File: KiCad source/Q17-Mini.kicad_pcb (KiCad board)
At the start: 2 copper layers, 95 x 75 mm, 85 parts, among them J1 Input, Q1 FQP3N30, Q10 KSA992, Q11 BS250P, Q12 BD139, Q13 FQP3N30, Q14 IRF9610, Q15 FQA46N15, Q16 FQA36P15, Q2 KSA992, Q3 KSC1845, Q4 FQP3P20, Q5 FQP3P20, Q6 FQP3N30, Q7 KSC1845, Q8 2N7000, Q9 BS250P, U1 OPA1641

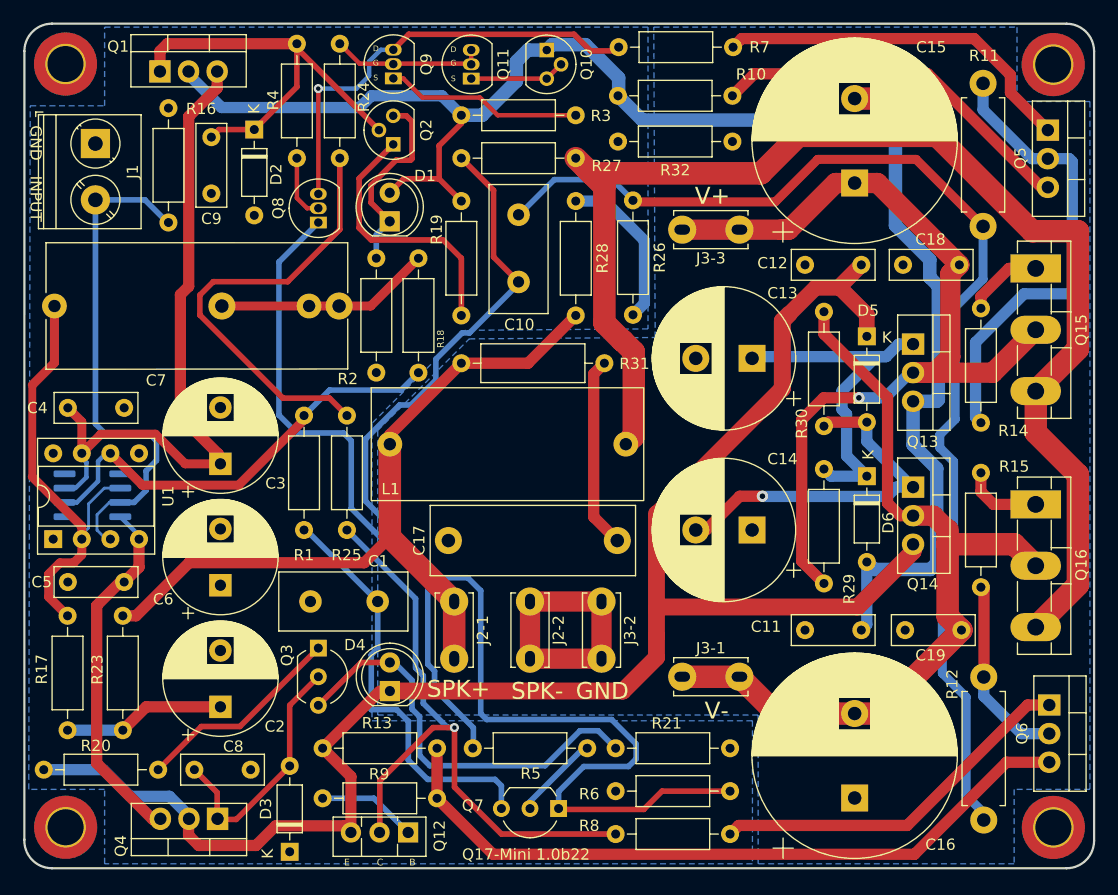
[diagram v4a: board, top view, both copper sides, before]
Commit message: Version 1.0
- Version 1.0 of Q17-Mini PCB.
- New footprint for C7 compatible with lead space of 15mm and 22.5mm.
- L1 adjusted to the correct inductance length of 22x10mm for 1.2uF (Wire: 1mm, Tube: 8mm interior, 22 turns).
- Gerber files for Q7-Mini 1.0.
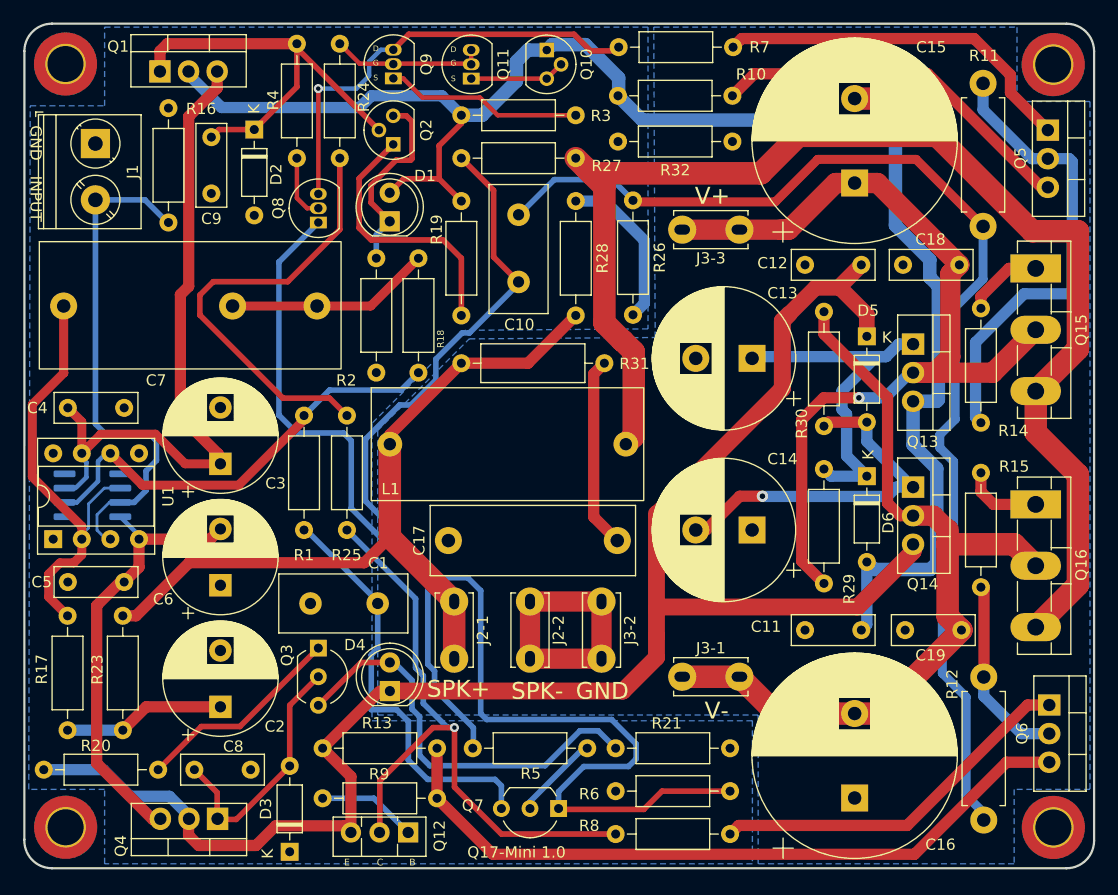
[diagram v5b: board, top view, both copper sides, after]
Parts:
- C7: footprint Capacitor_THT:C_Rect_L29.0mm_W11.0mm_P27.50mm_MKT_special -> Capacitor_THT:C_Rect_C7_Q17-Mini
- moved C7 0.94 mm to (103.3, 80.1)
- moved C1 0.18 mm to (131.1, 106.6)
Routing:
- net Net-(C5-Pad2): track 31.9 -> 39.5 mm
- net Net-(C7-Pad2): track 19.2 -> 18.3 mm
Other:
- board text added: "Q17-Mini 1.0"
- board text removed: "Q17-Mini 1.0b22"
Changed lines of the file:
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@@
     (title "Q17-Mini the Quad405 reborn")
     (date "2021-11-17")
-    (rev "1.0b22")
+    (rev "1.0")
     (company "PCB design by Stef")
     (comment 1 "Zize 95 x 75 mm")
-    (comment 2 "NO YET FINISHED - DO NOT PRINT")
   )
   (layers
@@
   )
   (footprint "Silver_Mica:C_Mica_L11.4mm_W4.3mm_H9.1_P5.9mm" (layer "F.Cu")
-    (at 131.128153 106.37722 180)
+    (at 131.128153 106.553 180)
     (descr "C, Silver Mica series, Radial, pin pitch=5.00mm, , diameter*width=11*5.0mm^2, Capacitor, http://www.vishay.com/docs/28535/vy2series.pdf")
     (tags "C Silver Mica series Radial pin pitch 5.00mm  diameter 11mm width 5.0mm Capacitor")
@@
     (property "Sheetname" "")
     (attr through_hole)
-    (fp_text reference "R2" (at 10.721294 2.539469) (layer "F.SilkS")
+    (fp_text reference "R2" (at 10.848294 2.666469) (layer "F.SilkS")
       (effects (font (size 1 1) (thickness 0.15)))
     )
@@
     )
   )
-  (footprint "Capacitor_THT:C_Rect_L29.0mm_W11.0mm_P27.50mm_MKT_special" (layer "F.Cu")
-    (at 102.362 80.137)
-    (descr "C, Rect series, Radial, pin pitch=22.00mm, , length*width=27*11mm^2, Capacitor")
-    (tags "C Rect series Radial pin pitch 22.00mm  length 27mm width 11mm Capacitor")
+  (footprint "Capacitor_THT:C_Rect_C7_Q17-Mini" (layer "F.Cu")
+    (at 103.299366 80.137)
+    (descr "C, Rect series, Radial, Q17 C7")
+    (tags "C Rect series Radial Q17 C7 Capacitor")
     (property "Sheetfile" "Q17-95x75.kicad_sch")
     (property "Sheetname" "")
     (attr through_hole)
-    (fp_text reference "C7" (at 9.144 6.604) (layer "F.SilkS")
-      (effects (font (size 1 1) (thickness 0.15)))
-    )
-    (fp_text value "1uF" (at 12.192 6.858) (layer "F.Fab")
-      (effects (font (size 1 1) (thickness 0.15)))
-    )
-    (fp_line (start 26.163827 5.589779) (end 26.163827 1.154779) (layer "F.SilkS") (width 0.12))
-    (fp_line (start -0.63 5.62) (end -0.63 1.185) (layer "F.SilkS") (width 0.12))
-    (fp_line (start -0.63 -1.185) (end -0.63 -5.62) (layer "F.SilkS") (width 0.12))
-    (fp_line (start 26.163827 -1.179624) (end 26.163827 -5.614624) (layer "F.SilkS") (width 0.12))
-    (fp_line (start 26.163827 5.589779) (end -0.63 5.62) (layer "F.SilkS") (width 0.12))
-    (fp_line (start 26.163827 -5.614624) (end -0.63 -5.62) (layer "F.SilkS") (width 0.12))
-    (fp_line (start 26.924 -5.75) (end -1.21 -5.75) (layer "F.CrtYd") (width 0.05))
-    (fp_line (start 26.924 5.75) (end 26.924 -5.75) (layer "F.CrtYd") (width 0.05))
-    (fp_line (start -1.21 5.75) (end 26.924 5.75) (layer "F.CrtYd") (width 0.05))
-    (fp_line (start -1.21 -5.75) (end -1.21 5.75) (layer "F.CrtYd") (width 0.05))
-    (fp_line (start -0.51 -5.5) (end -0.51 5.5) (layer "F.Fab") (width 0.1))
-    (fp_line (start 26.029947 -5.474709) (end -0.51 -5.5) (layer "F.Fab") (width 0.1))
-    (fp_line (start 26.029947 5.525291) (end 26.029947 -5.474709) (layer "F.Fab") (width 0.1))
-    (fp_line (start -0.51 5.5) (end 26.029947 5.525291) (layer "F.Fab") (width 0.1))
-    (pad "1" thru_hole circle (at 0.12 0) (size 2.2 2.2) (drill 1.1) (layers *.Cu *.Mask)
+    (fp_text reference "C7" (at 8.206634 6.604) (layer "F.SilkS")
+      (effects (font (size 1 1) (thickness 0.15)))
+    )
+    (fp_text value "1uF" (at 11.049 7.239) (layer "F.Fab")
+      (effects (font (size 1 1) (thickness 0.15)))
+    )
+    (fp_text user "${REFERENCE}" (at 8.255 0) (layer "F.Fab")
+      (effects (font (size 1 1) (thickness 0.15)))
+    )
+    (fp_rect (start -2.159 -5.715) (end 24.638 5.588) (layer "F.SilkS") (width 0.12) (fill none))
+    (fp_rect (start -2.255731 -5.825894) (end 24.765 5.715) (layer "F.CrtYd") (width 0.05) (fill none))
+    (fp_rect (start -2.032 -5.539) (end 24.476 5.461) (layer "F.Fab") (width 0.12) (fill none))
+    (pad "1" thru_hole circle (at 0 0) (size 2.4 2.4) (drill 1.2) (layers *.Cu *.Mask)
       (net 6 "Net-(C7-Pad1)"))
-    (pad "2" thru_hole circle (at 25.4 0 180) (size 2.4 2.4) (drill 1.2) (layers *.Cu *.Mask)
-      (net 7 "Net-(C7-Pad2)"))
-    (pad "3" thru_hole circle (at 22.733 0) (size 2.2 2.2) (drill 1.1) (layers *.Cu *.Mask)
+    (pad "2" thru_hole circle (at 22.5 0) (size 2.4 2.4) (drill 1.2) (layers *.Cu *.Mask)
       (net 7 "Net-(C7-Pad2)"))
-    (pad "4" thru_hole circle (at 14.986 0 180) (size 2.4 2.4) (drill 1.2) (layers *.Cu *.Mask)
+    (pad "3" thru_hole circle (at 15 0 180) (size 2.4 2.4) (drill 1.2) (layers *.Cu *.Mask)
       (net 7 "Net-(C7-Pad2)"))
-    (model "${KICAD6_3DMODEL_DIR}/Capacitor_THT.3dshapes/C_Rect_L27.0mm_W11.0mm_P22.00mm.wrl"
+    (model "/Users/sleclerc/Library/Application Support/kicad/3dmodels/Capacitor_THT.3dshapes/C_Rect_L26.5mm_W10.5mm_P22.50mm_MKS4.wrl"
       (offset (xyz 0 0 0))
       (scale (xyz 1 1 1))
@@
   (gr_arc (start 100.001478 57.547161) (mid 100.743435 55.860377) (end 102.488475 55.268284) (layer "Margin") (width 0.2))
   (gr_arc (start 194.60834 127.475319) (mid 193.978178 129.188795) (end 192.280626 129.860674) (layer "Margin") (width 0.2))
-  (gr_line (start 121.285 93.726) (end 121.285 119.888) (layer "User.2") (width 0.12))
   (gr_text "GND" (at 147.877574 108.966) (layer "B.SilkS")
     (effects (font (size 1.5 1.5) (thickness 0.3)) (justify mirror))
@@
     (effects (font (size 0.5 0.5) (thickness 0.125)))
   )
-  (gr_text "Q17-Mini 1.0b22" (at 144.355041 128.83975) (layer "F.SilkS")
+  (gr_text "Q17-Mini 1.0" (at 143.51 128.651) (layer "F.SilkS")
     (effects (font (size 1 1) (thickness 0.25)))
   )
@@
   (segment (start 105.320999 94.017999) (end 104.521 93.218) (width 0.4) (layer "B.Cu") (net 4))
   (segment (start 109.992 103.328) (end 109.992 100.838) (width 1) (layer "F.Cu") (net 5))
+  (segment (start 109.992 100.838) (end 116.317897 100.838) (width 1) (layer "F.Cu") (net 5))
   (segment (start 106.231041 106.743701) (end 108.326742 104.648) (width 1) (layer "F.Cu") (net 5))
   (segment (start 108.672 104.648) (end 109.992 103.328) (width 1) (layer "F.Cu") (net 5))
   (segment (start 106.231041 120.740987) (end 106.231041 106.743701) (width 1) (layer "F.Cu") (net 5))
+  (segment (start 116.317897 100.838) (end 117.221 99.934897) (width 1) (layer "F.Cu") (net 5))
   (segment (start 111.220054 125.73) (end 106.231041 120.740987) (width 1) (layer "F.Cu") (net 5))
   (segment (start 108.326742 104.648) (end 108.672 104.648) (width 1) (layer "F.Cu") (net 5))
@@
   (segment (start 102.968038 102.948489) (end 104.188511 102.948489) (width 0.8) (layer "F.Cu") (net 6))
   (segment (start 104.188511 102.948489) (end 104.912 102.225) (width 0.8) (layer "F.Cu") (net 6))
-  (segment (start 102.482 85.183461) (end 100.516041 87.14942) (width 0.8) (layer "F.Cu") (net 6))
-  (segment (start 100.516041 87.14942) (end 100.516041 95.309041) (width 0.7) (layer "F.Cu") (net 6))
+  (segment (start 103.299366 86.065998) (end 103.299366 80.137) (width 0.8) (layer "F.Cu") (net 6))
+  (segment (start 100.516041 95.309041) (end 100.516041 88.878003) (width 0.8) (layer "F.Cu") (net 6))
   (segment (start 104.912 99.705) (end 100.516041 95.309041) (width 0.8) (layer "F.Cu") (net 6))
+  (segment (start 103.313706 86.080338) (end 103.299366 86.065998) (width 0.8) (layer "F.Cu") (net 6))
   (segment (start 101.972489 103.944038) (end 102.968038 102.948489) (width 0.8) (layer "F.Cu") (net 6))
-  (segment (start 102.482 80.137) (end 102.482 85.183461) (width 0.8) (layer "F.Cu") (net 6))
+  (segment (start 100.516041 88.878003) (end 103.313706 86.080338) (width 0.8) (layer "F.Cu") (net 6))
   (segment (start 101.972489 105.97299) (end 101.972489 103.944038) (width 0.8) (layer "F.Cu") (net 6))
   (segment (start 104.912 102.225) (end 104.912 99.705) (width 0.8) (layer "F.Cu") (net 6))
@@
   (segment (start 106.911995 96.308097) (end 108.329717 96.308097) (width 0.25) (layer "B.Cu") (net 6))
   (segment (start 105.511481 97.708611) (end 106.911995 96.308097) (width 0.25) (layer "B.Cu") (net 6))
-  (segment (start 127.762 80.137) (end 117.348 80.137) (width 0.8) (layer "F.Cu") (net 7))
-  (segment (start 127.762 80.137) (end 130.566261 80.137) (width 0.8) (layer "F.Cu") (net 7))
+  (segment (start 130.566261 80.137) (end 118.299366 80.137) (width 0.8) (layer "F.Cu") (net 7))
   (segment (start 130.566261 80.137) (end 134.806041 75.89722) (width 0.8) (layer "F.Cu") (net 7))
   (segment (start 116.931041 125.73) (end 118.628261 125.73) (width 0.5) (layer "F.Cu") (net 8))

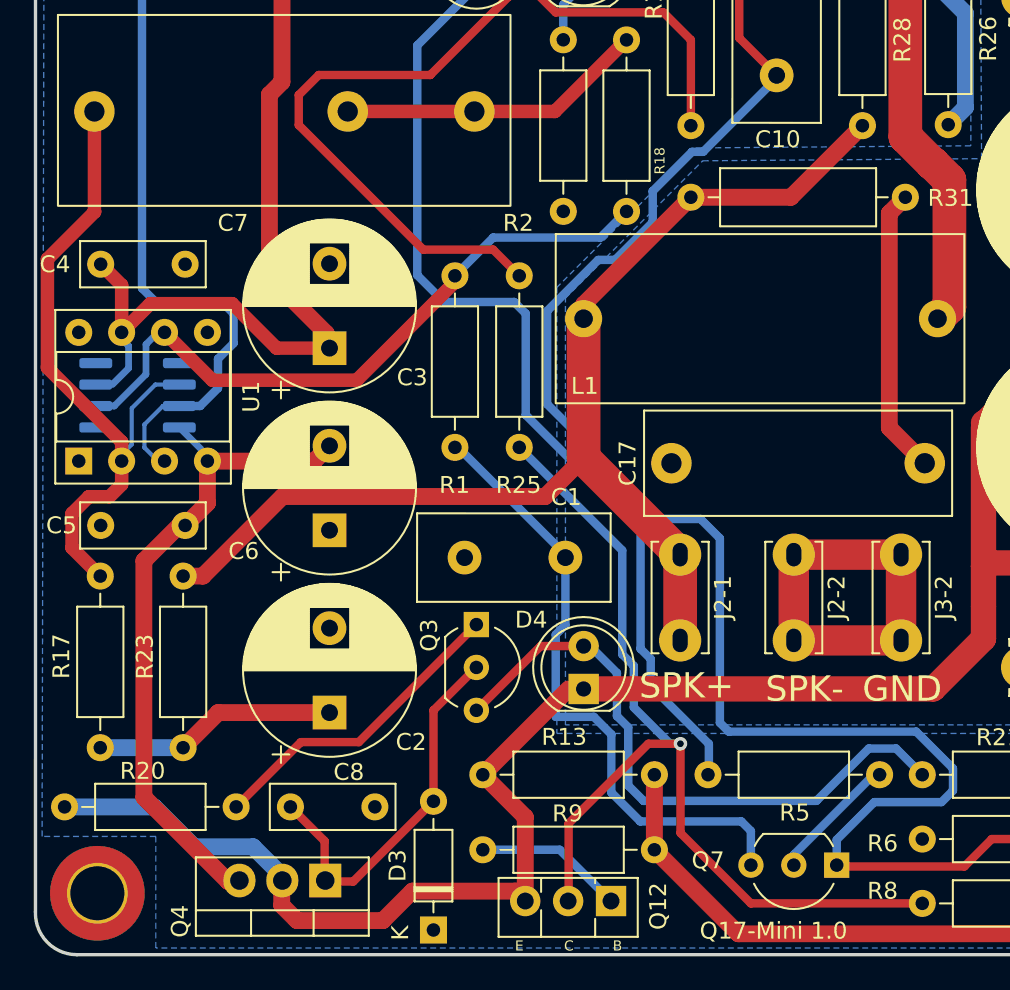
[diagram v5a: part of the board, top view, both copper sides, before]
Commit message: Version 1.0.1
- Wrong hole size for C7.
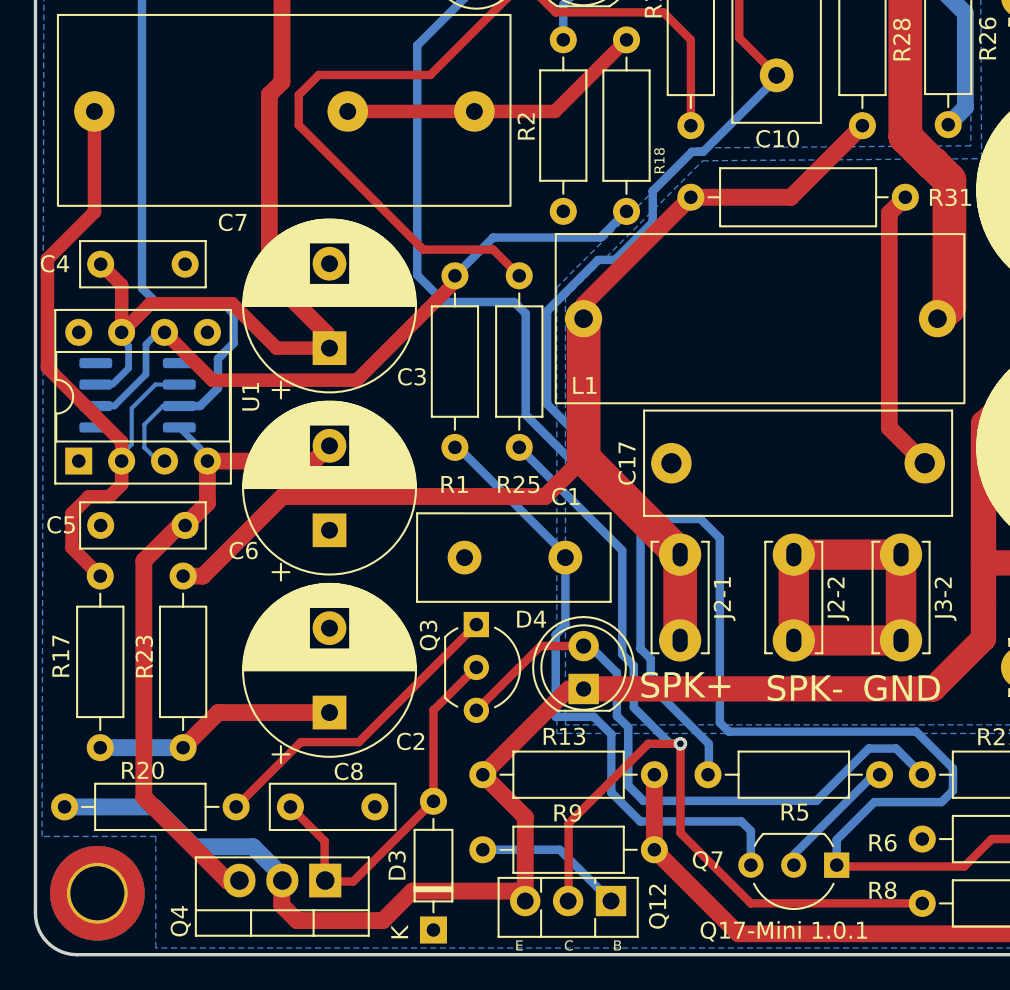
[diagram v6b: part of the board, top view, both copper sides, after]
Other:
- board text added: "Q17-Mini 1.0.1"
- board text removed: "Q17-Mini 1.0"
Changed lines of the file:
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@@
   (title_block
     (title "Q17-Mini the Quad405 reborn")
-    (date "2021-11-17")
-    (rev "1.0")
+    (date "2021-11-18")
+    (rev "1.0.1")
     (company "PCB design by Stef")
     (comment 1 "Zize 95 x 75 mm")
@@
     (property "Sheetname" "")
     (attr through_hole)
-    (fp_text reference "R2" (at 10.848294 2.666469) (layer "F.SilkS")
+    (fp_text reference "R2" (at 5.133294 2.158469 -90) (layer "F.SilkS")
       (effects (font (size 1 1) (thickness 0.15)))
     )
@@
     (fp_rect (start -2.255731 -5.825894) (end 24.765 5.715) (layer "F.CrtYd") (width 0.05) (fill none))
     (fp_rect (start -2.032 -5.539) (end 24.476 5.461) (layer "F.Fab") (width 0.12) (fill none))
-    (pad "1" thru_hole circle (at 0 0) (size 2.4 2.4) (drill 1.2) (layers *.Cu *.Mask)
+    (pad "1" thru_hole circle (at 0 0) (size 2.4 2.4) (drill 1) (layers *.Cu *.Mask)
       (net 6 "Net-(C7-Pad1)"))
-    (pad "2" thru_hole circle (at 22.5 0) (size 2.4 2.4) (drill 1.2) (layers *.Cu *.Mask)
+    (pad "2" thru_hole circle (at 22.5 0) (size 2.4 2.4) (drill 1) (layers *.Cu *.Mask)
       (net 7 "Net-(C7-Pad2)"))
-    (pad "3" thru_hole circle (at 15 0 180) (size 2.4 2.4) (drill 1.2) (layers *.Cu *.Mask)
+    (pad "3" thru_hole circle (at 15 0 180) (size 2.4 2.4) (drill 1) (layers *.Cu *.Mask)
       (net 7 "Net-(C7-Pad2)"))
     (model "/Users/sleclerc/Library/Application Support/kicad/3dmodels/Capacitor_THT.3dshapes/C_Rect_L26.5mm_W10.5mm_P22.50mm_MKS4.wrl"
@@
     (effects (font (size 0.5 0.5) (thickness 0.125)))
   )
-  (gr_text "Q17-Mini 1.0" (at 143.51 128.651) (layer "F.SilkS")
+  (gr_text "Q17-Mini 1.0.1" (at 144.145 128.651) (layer "F.SilkS")
     (effects (font (size 1 1) (thickness 0.25)))
   )
